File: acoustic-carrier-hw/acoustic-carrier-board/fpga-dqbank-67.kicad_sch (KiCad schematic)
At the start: 8 parts, among them IC1 ECP5-BGA256

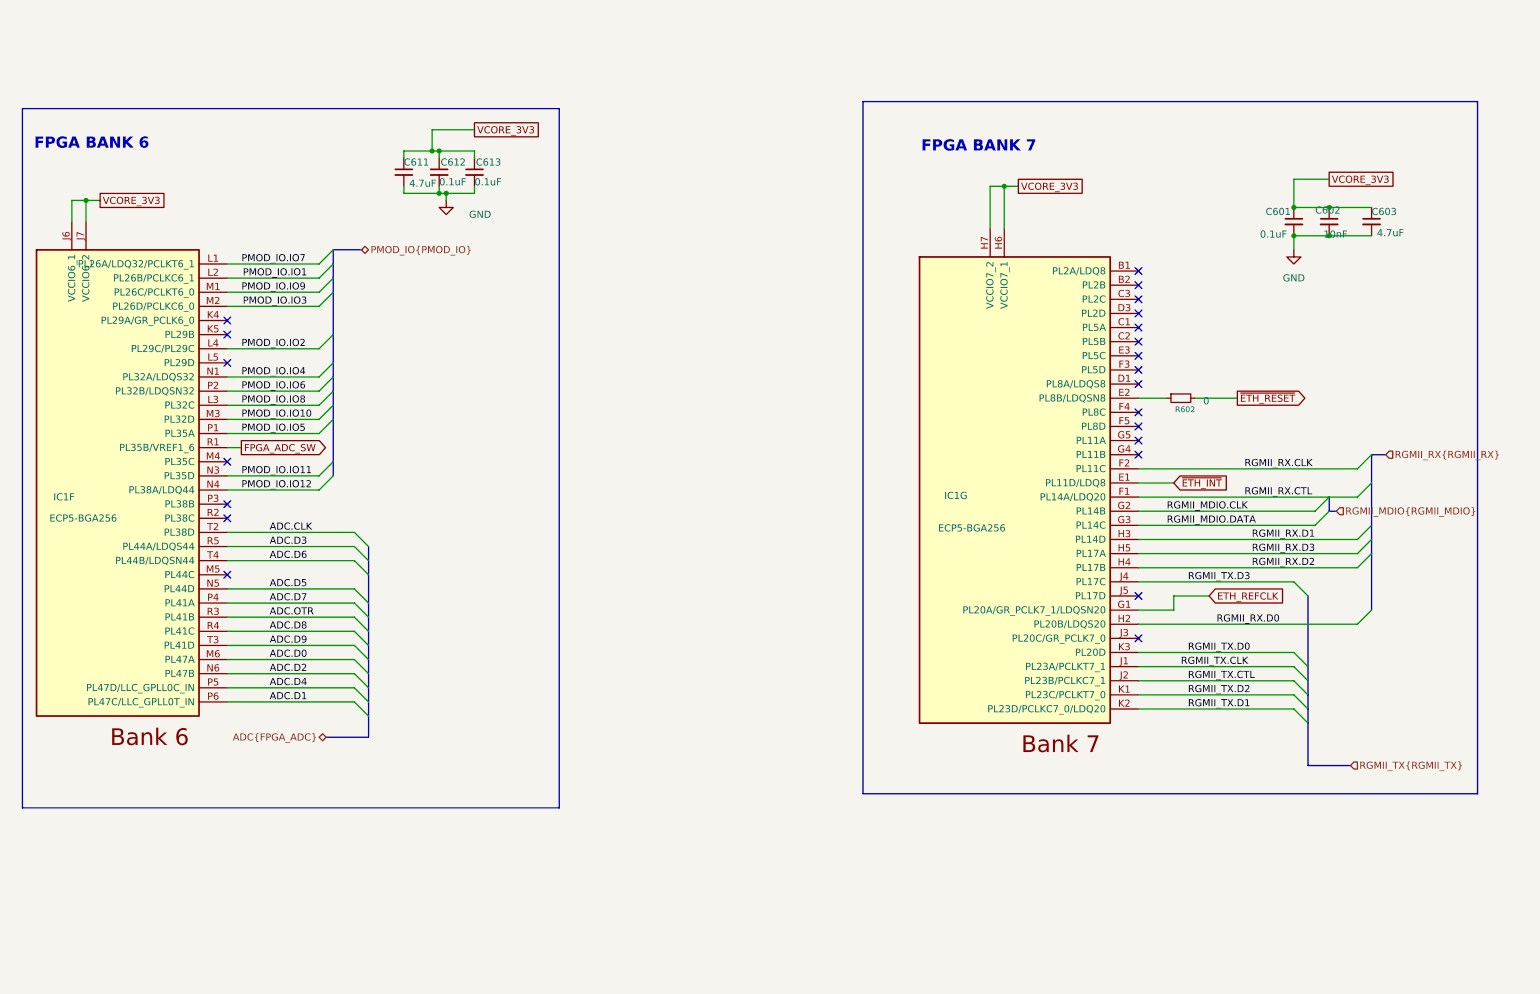
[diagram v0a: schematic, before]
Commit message: [carrier] Added 2 buttons and 2 leds + routing
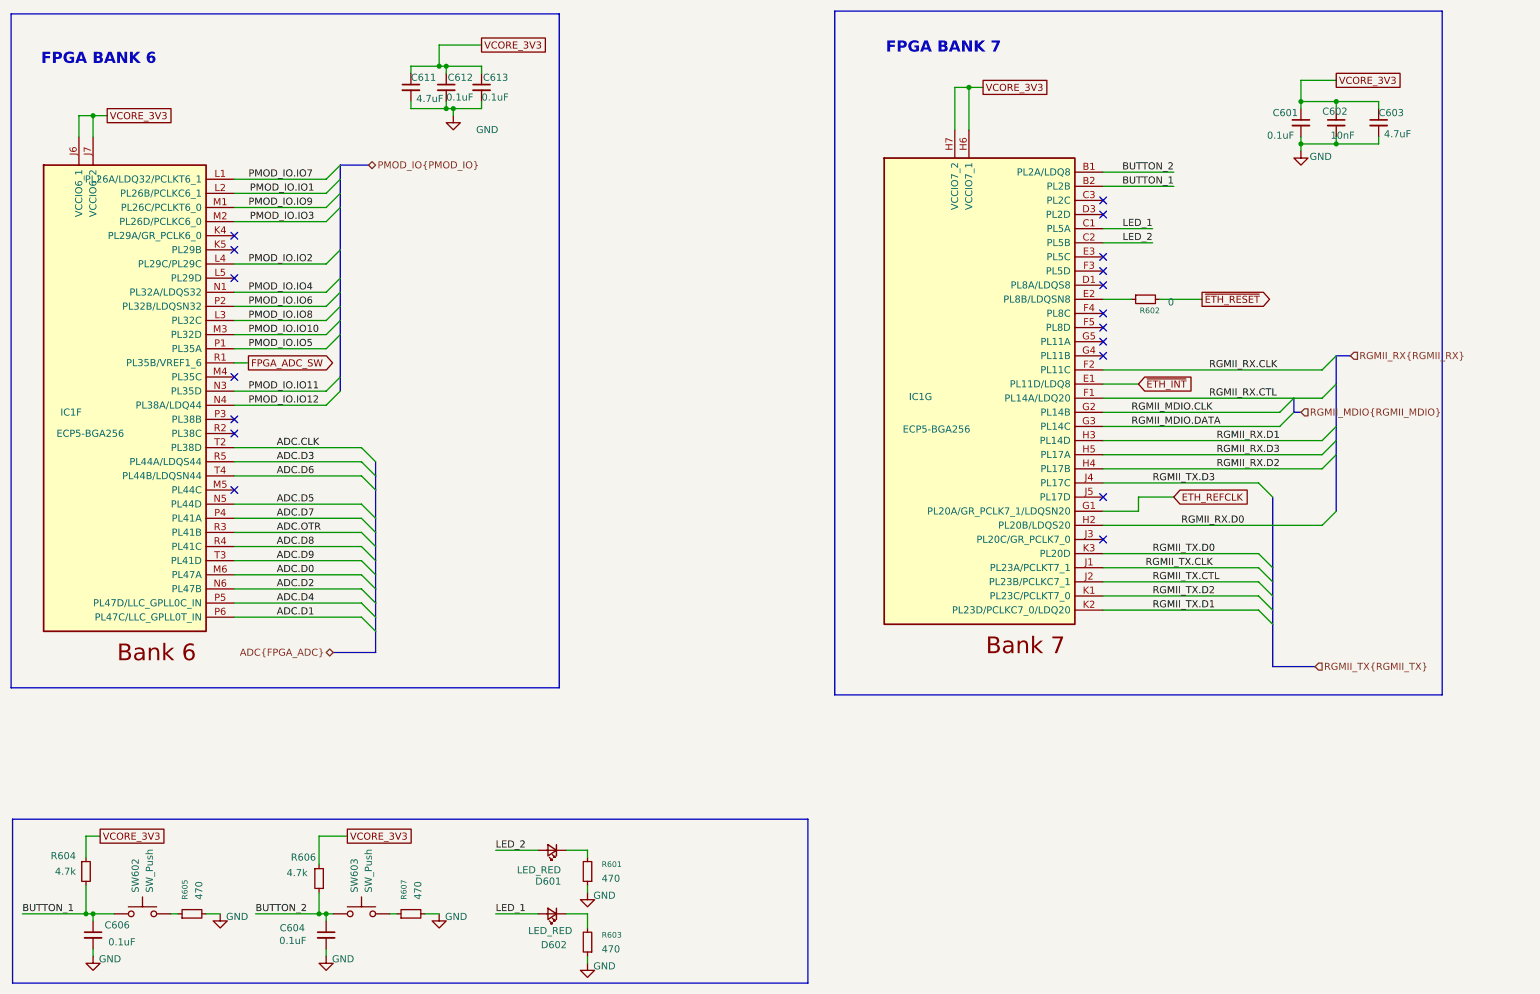
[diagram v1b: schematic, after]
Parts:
- added C604, C606: 0.1uF, Capacitor_SMD:C_0201_0603Metric, symbol Device:C_Small
- added D601, D602: LED_RED, LED_SMD:LED_0603_1608Metric, symbol Device:LED_Small
- added R601, R603, R605, R607: 470, Resistor_SMD:R_0402_1005Metric, symbol Device:R_Small
- added R604, R606: 4.7k, Resistor_SMD:R_0402_1005Metric, symbol Device:R_Small
- added SW602, SW603: SW_Push, iw-misc:SW_TS-1088-AR02016, symbol Switch:SW_Push
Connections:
- net GND: now also C604.2, C606.2, R601.1, R603.1, R605.2, R607.2
- net VCORE_3V3: now also R604.1, R606.1
- net BUTTON_2: now reaches IC1.B1 (PL2A/LDQ8)
- net BUTTON_2: now also C604.1, R606.2, SW603.1
- net BUTTON_1: now reaches IC1.B2 (PL2B)
- net BUTTON_1: now also C606.1, R604.2, SW602.1
- net LED_1: now reaches IC1.C1 (PL5A)
- net LED_1: now also D602.2 (A)
- net LED_2: now reaches IC1.C2 (PL5B)
- net LED_2: now also D601.2 (A)
- new net: R607.1, SW603.2
- new net: R605.1, SW602.2
- new net: D601.1 (K), R601.2
- new net: D602.1 (K), R603.2
- no-connect marks 22 -> 18
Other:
- moved on the sheet: C601, C602, C603, C611, C612, C613, IC1F, IC1G, R602

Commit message: [carrier] finished for production (next) reroute the LPDDR3, with appropriate CMD-CTRL bus delays, and change banks for command-control
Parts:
- IC1: Manufacturer Lattice -> (none)
